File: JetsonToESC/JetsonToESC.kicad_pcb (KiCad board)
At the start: 2 copper layers, 32 x 47.5 mm, 8 parts, among them J1 Conn_01x12, J2 Conn_01x03, U1 ESP32-C3_SUPERMINI_TH, U2 DS18B20

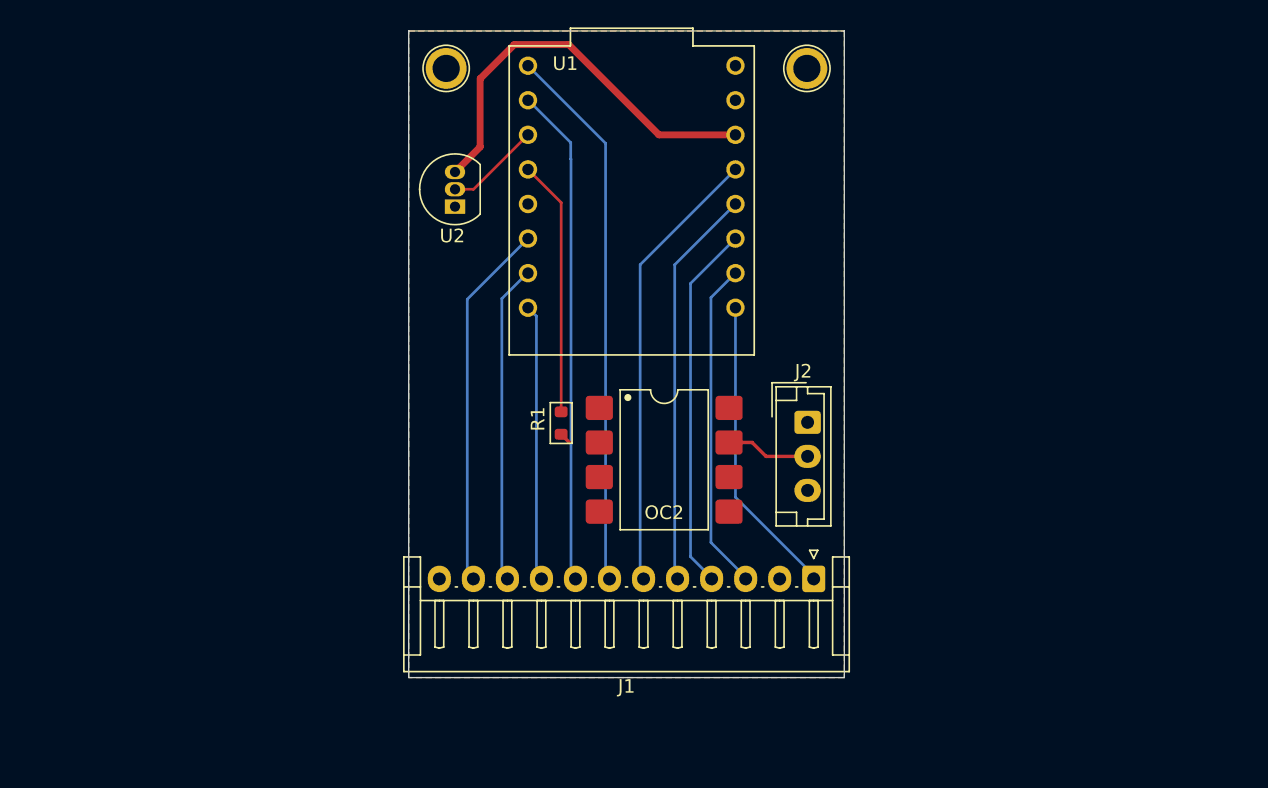
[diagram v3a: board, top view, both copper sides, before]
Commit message: Design almost finished, added hierarchical sheets
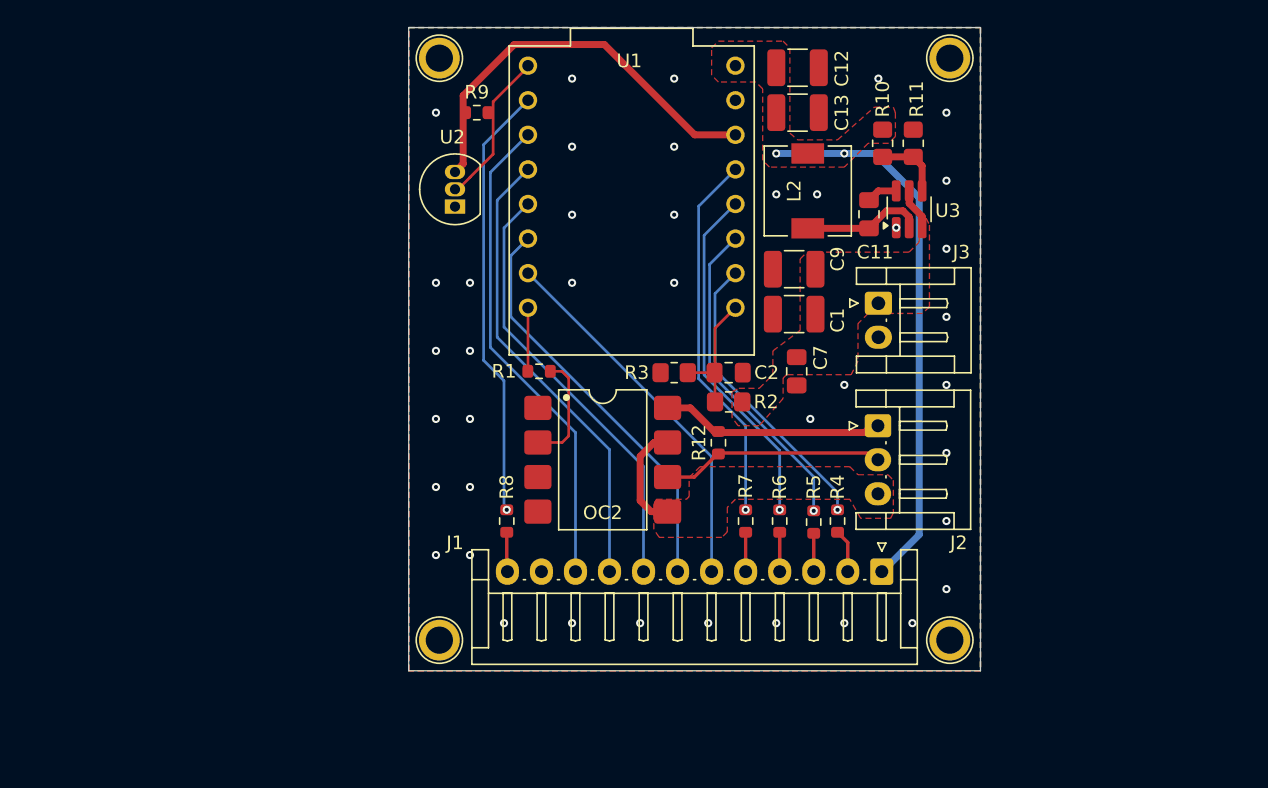
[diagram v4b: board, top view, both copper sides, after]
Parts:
- added C1: 4.7uF, Capacitor_SMD:C_1210_3225Metric_Pad1.33x2.70mm_HandSolder, F.Cu at (166.3, 99.8)
- added C11: 100nF, Capacitor_SMD:C_0805_2012Metric_Pad1.18x1.45mm_HandSolder, F.Cu at (171.8, 92.5)
- added C12: 22uF, Capacitor_SMD:C_1210_3225Metric_Pad1.33x2.70mm_HandSolder, F.Cu at (166.6, 81.7)
- added C13: 22uF, Capacitor_SMD:C_1210_3225Metric_Pad1.33x2.70mm_HandSolder, F.Cu at (166.6, 85.0)
- added C2: 100nF, Capacitor_SMD:C_0805_2012Metric_Pad1.18x1.45mm_HandSolder, F.Cu at (161.5, 104.1)
- added C7: 100nF, Capacitor_SMD:C_0805_2012Metric_Pad1.18x1.45mm_HandSolder, F.Cu at (166.5, 104.0)
- added C9: 4.7uF, Capacitor_SMD:C_1210_3225Metric_Pad1.33x2.70mm_HandSolder, F.Cu at (166.3, 96.5)
- added H3: MountingHole, TestPoint:TestPoint_Plated_Hole_D2.0mm, F.Cu at (140.2, 123.8)
- added H4: MountingHole, TestPoint:TestPoint_Plated_Hole_D2.0mm, F.Cu at (177.8, 123.8)
- added J3: Conn_01x02, Connector_JST:JST_EH_S2B-EH_1x02_P2.50mm_Horizontal, F.Cu at (172.5, 99.0)
- added L2: 6.8uH, Inductor_SMD:L_6.3x6.3_H3, F.Cu at (167.3, 90.8)
- added R10: 100k, Resistor_SMD:R_0805_2012Metric_Pad1.20x1.40mm_HandSolder, F.Cu at (172.8, 87.2)
- added R11: 13.7k, Resistor_SMD:R_0805_2012Metric_Pad1.20x1.40mm_HandSolder, F.Cu at (175.1, 87.2)
- added R12: 4K7, Resistor_SMD:R_0603_1608Metric, F.Cu at (160.8, 109.2)
- added R2: 47K, Resistor_SMD:R_0805_2012Metric_Pad1.20x1.40mm_HandSolder, F.Cu at (161.5, 106.2)
- added R3: 5.1K, Resistor_SMD:R_0805_2012Metric_Pad1.20x1.40mm_HandSolder, F.Cu at (157.5, 104.1)
- added R4: 4K7, Resistor_SMD:R_0603_1608Metric, F.Cu at (169.5, 115.0)
- added R5: 4K7, Resistor_SMD:R_0603_1608Metric, F.Cu at (167.8, 115.1)
- added R6: 4K7, Resistor_SMD:R_0603_1608Metric, F.Cu at (165.2, 115.0)
- added R7: 4K7, Resistor_SMD:R_0603_1608Metric, F.Cu at (162.8, 115.0)
- added R8: 4K7, Resistor_SMD:R_0603_1608Metric, F.Cu at (145.2, 115.0)
- added R9: 4K7, Resistor_SMD:R_0603_1608Metric, F.Cu at (143.0, 85.0)
- added U3: LMR51420XDDCR, Package_TO_SOT_SMD:SOT-23-6_Handsoldering, F.Cu at (174.8, 92.1)
- J2: footprint Connector_JST:JST_EH_B3B-EH-A_1x03_P2.50mm_Vertical -> Connector_JST:JST_EH_S3B-EH_1x03_P2.50mm_Horizontal
- R1: value R -> 220; footprint PCM_Resistor_SMD_AKL:R_0603_1608Metric -> Resistor_SMD:R_0603_1608Metric
- moved H2 10.5 mm to (177.8, 81.0)
- moved J2 5.17 mm to (172.5, 108.0)
- moved J1 5.03 mm to (172.8, 118.7)
- moved OC2 4.51 mm to (152.2, 110.5)
- moved R1 4.13 mm to (147.6, 104.0), turned to 0 degrees
- moved H1 0.90 mm to (140.2, 81.0)
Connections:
- J1 pad 1: LED_TEMP -> 5V
- J1 pad 10: LED_BATT_MED -> BUTTON_STOP
- J1 pad 11: LED_BATT_LOW -> GND
- J1 pad 12: 5V -> LED_TEMP
- J1 pad 2: GND -> LED_BATT_LOW
- J1 pad 3: BUTTON_STOP -> LED_BATT_MED
- J1 pad 4: BUTTON_25% -> LED_BATT_HI
- J1 pad 5: BUTTON_50% -> LED_OVERCURRENT
- J1 pad 6: BUTTON_75% -> BUTTON_100%
- J1 pad 7: BUTTON_100% -> BUTTON_75%
- J1 pad 8: LED_OVERCURRENT -> BUTTON_50%
- J1 pad 9: LED_BATT_HI -> BUTTON_25%
- J2 pad 1: VCC -> VBEC
- J2 pad 3: GND -> GNDB
- OC2 pad 5: GND -> GNDB
- OC2 pad 6: unconnected-(OC2-Pad6) -> ESC_PWM
- OC2 pad 7: ESC_PWM -> GNDB
- OC2 pad 8: VCC -> VBEC
- U1 pad 0: LED_TEMP -> BATT_LEVEL_SENSE
- U1 pad 1: BUTTON_STOP -> Net-(U1-GPIO1)
- U1 pad 10: LED_BATT_LOW -> BUTTON_75%
- U1 pad 2: BUTTON_25% -> Net-(U1-GPIO2)
- U1 pad 20: LED_BATT_MED -> BUTTON_100%
- U1 pad 21: LED_BATT_HI -> PWM
- U1 pad 3: BUTTON_50% -> Net-(U1-GPIO3)
- U1 pad 4: BUTTON_75% -> Net-(U1-GPIO4)
- U1 pad 5: BUTTON_100% -> TEMP_SENSE
- U1 pad 5V: VCC -> 5V
- U1 pad 6: LED_OVERCURRENT -> Net-(U1-GPIO6)
- U1 pad 7: TEMP_SENSE -> BUTTON_STOP
- U1 pad 8: PWM -> BUTTON_25%
- U1 pad 9: unconnected-(U1-GPIO9-Pad9) -> BUTTON_50%
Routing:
- net 5V: track 0.00 -> 40.5 mm, vias 0 -> 2
- net LED_OVERCURRENT: track 36.2 -> 2.89 mm
- net Net-(U1-GPIO6): track 0.00 -> 32.2 mm, vias 0 -> 1
- net Net-(U1-GPIO4): track 0.00 -> 27.6 mm, vias 0 -> 1
- net Net-(U1-GPIO3): track 0.00 -> 25.7 mm, vias 0 -> 1
- net Net-(U1-GPIO2): track 0.00 -> 24.0 mm, vias 0 -> 1
- net LED_BATT_LOW: track 26.6 -> 3.20 mm
- net Net-(U1-GPIO1): track 0.00 -> 21.9 mm, vias 0 -> 1
- net LED_BATT_MED: track 23.0 -> 2.87 mm
- net LED_TEMP: track 22.0 -> 2.91 mm
- net LED_BATT_HI: track 19.9 -> 2.89 mm
- net VBEC: track 0.00 -> 16.4 mm
- net PWM: track 18.8 -> 4.67 mm
- net BUTTON_STOP: track 24.0 -> 36.8 mm
- net BUTTON_100%: track 39.8 -> 28.6 mm
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- added copper zone on F.Cu, net 5V
- added copper zone on F.Cu, net GNDB
- added copper zone on F.Cu, net VBAT
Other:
- board size 32 x 47.5 mm -> 42 x 47.2 mm

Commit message: Start On this Branch
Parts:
- added C3: 100nF, Capacitor_SMD:C_0805_2012Metric_Pad1.18x1.45mm_HandSolder, F.Cu at (117.6, 88.9)
- added R13: 4K7, Resistor_SMD:R_0603_1608Metric, F.Cu at (120.4, 89.3)
- added U4: MCP23018x-x-SS, Package_SO:SSOP-24_5.3x8.2mm_P0.65mm, F.Cu at (194.7, 126.5)
- added U5: ACS759xCB-100B-PFF, Sensor_Current:Allegro_CB_PFF, F.Cu at (141.3, 103.5)

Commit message: Work on current sense and io expansion branch
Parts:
- C11, C2, C7: footprint Capacitor_SMD:C_0805_2012Metric_Pad1.18x1.45mm_HandSolder -> Capacitor_SMD:C_0603_1608Metric
- R2, R3: footprint Resistor_SMD:R_0805_2012Metric_Pad1.20x1.40mm_HandSolder -> Resistor_SMD:R_0603_1608Metric
- moved U4 46.6 mm to (149.6, 114.8), turned to -90 degrees
- moved H3 28.0 mm to (112.5, 127.5)
- moved H1 27.8 mm to (112.5, 82.5)
- moved OC2 10.1 mm to (162.2, 111.8)
- moved R12 8.84 mm to (169.5, 110.5)
- moved R3 5.51 mm to (163.0, 104.5), turned to 90 degrees
- moved R2 5.40 mm to (166.8, 105.2)
- moved R6 4.86 mm to (162.5, 119.0)
- moved R7 4.85 mm to (160.0, 119.0)
- moved R5 4.80 mm to (165.0, 119.0)
- moved J1 4.68 mm to (170.0, 122.5)
- moved R4 4.47 mm to (167.5, 119.0)
- moved H4 3.76 mm to (177.5, 127.5)
- moved U2 3.05 mm to (138.6, 93.2)
- moved U5 3.05 mm to (138.5, 104.8)
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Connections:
- R4 pad 1: LED_BATT_LOW -> LED_OVERCURRENT
- R4 pad 2: Net-(U1-GPIO1) -> Net-(U4-GPB3)
- R5 pad 1: LED_BATT_MED -> LED_OVERCURRENT
- R5 pad 2: Net-(U1-GPIO2) -> Net-(U4-GPB4)
- R6 pad 2: Net-(U1-GPIO3) -> Net-(U4-GPB5)
- R7 pad 1: LED_OVERCURRENT -> LED_BATT_MED
- R7 pad 2: Net-(U1-GPIO4) -> Net-(U4-GPB6)
- R8 pad 1: LED_TEMP -> LED_BATT_LOW
- R8 pad 2: Net-(U1-GPIO6) -> Net-(U4-GPB7)
- U1 pad 1: Net-(U1-GPIO1) -> unconnected-(U1-GPIO1-Pad1)
- U1 pad 10: BUTTON_75% -> unconnected-(U1-GPIO10-Pad10)
- U1 pad 2: Net-(U1-GPIO2) -> unconnected-(U1-GPIO2-Pad2)
- U1 pad 20: BUTTON_100% -> unconnected-(U1-GPIO20-Pad20)
- U1 pad 3: Net-(U1-GPIO3) -> unconnected-(U1-GPIO3-Pad3)
- U1 pad 4: Net-(U1-GPIO4) -> unconnected-(U1-GPIO4-Pad4)
- U1 pad 6: Net-(U1-GPIO6) -> unconnected-(U1-GPIO6-Pad6)
- U1 pad 7: BUTTON_STOP -> unconnected-(U1-GPIO7-Pad7)
- U1 pad 8: BUTTON_25% -> I2C_SDA
- U1 pad 9: BUTTON_50% -> I2C_SCL
- U4 pad 5: LED_OVERCURRENT -> Net-(U4-GPB3)
- U4 pad 6: LED_OVERCURRENT -> Net-(U4-GPB4)
- U4 pad 7: LED_BATT_HI -> Net-(U4-GPB5)
- U4 pad 8: LED_BATT_MED -> Net-(U4-GPB6)
- U4 pad 9: LED_BATT_LOW -> Net-(U4-GPB7)
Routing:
- net BUTTON_STOP: track 36.8 -> 0.00 mm
- net BUTTON_25%: track 34.4 -> 0.00 mm
- net BUTTON_50%: track 33.0 -> 0.00 mm
- net Net-(U1-GPIO6): track 32.2 -> 0.00 mm, vias 1 -> 0
- net BUTTON_75%: track 30.3 -> 0.00 mm
- net BUTTON_100%: track 28.6 -> 0.00 mm
- net Net-(U1-GPIO4): track 27.6 -> 0.00 mm, vias 1 -> 0
- net Net-(U1-GPIO3): track 25.7 -> 0.00 mm, vias 1 -> 0
- net Net-(U1-GPIO2): track 24.0 -> 0.00 mm, vias 1 -> 0
- net Net-(U1-GPIO1): track 21.9 -> 0.00 mm, vias 1 -> 0
- net VBEC: track 16.4 -> 0.00 mm
- net ESC_PWM: track 16.4 -> 0.00 mm
- net Net-(OC2-Pad2): track 8.27 -> 0.00 mm
- net GNDB: track 8.25 -> 0.00 mm
- net 5V: track 40.5 -> 45.6 mm
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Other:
- board size 42 x 47.2 mm -> 70 x 50 mm

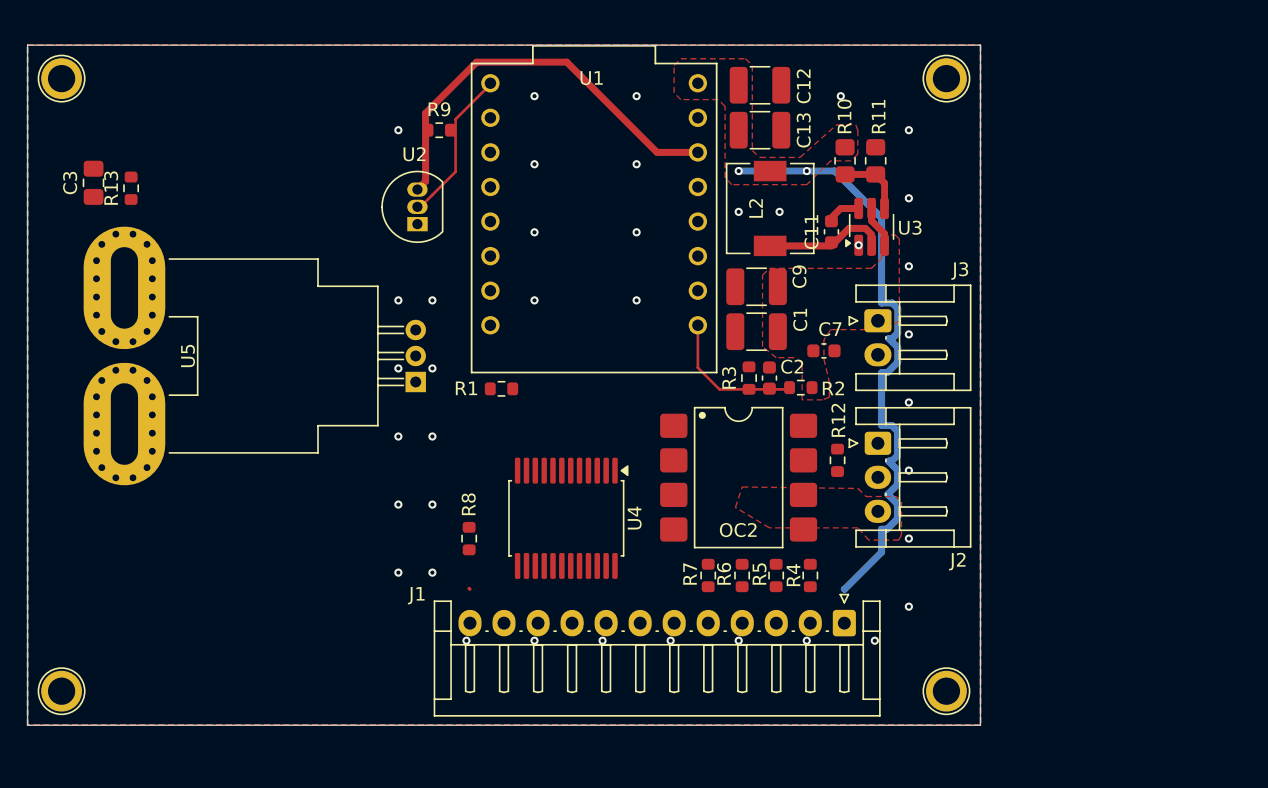
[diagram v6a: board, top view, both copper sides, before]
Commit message: Updated routing for IO Expander and Hall Sensor
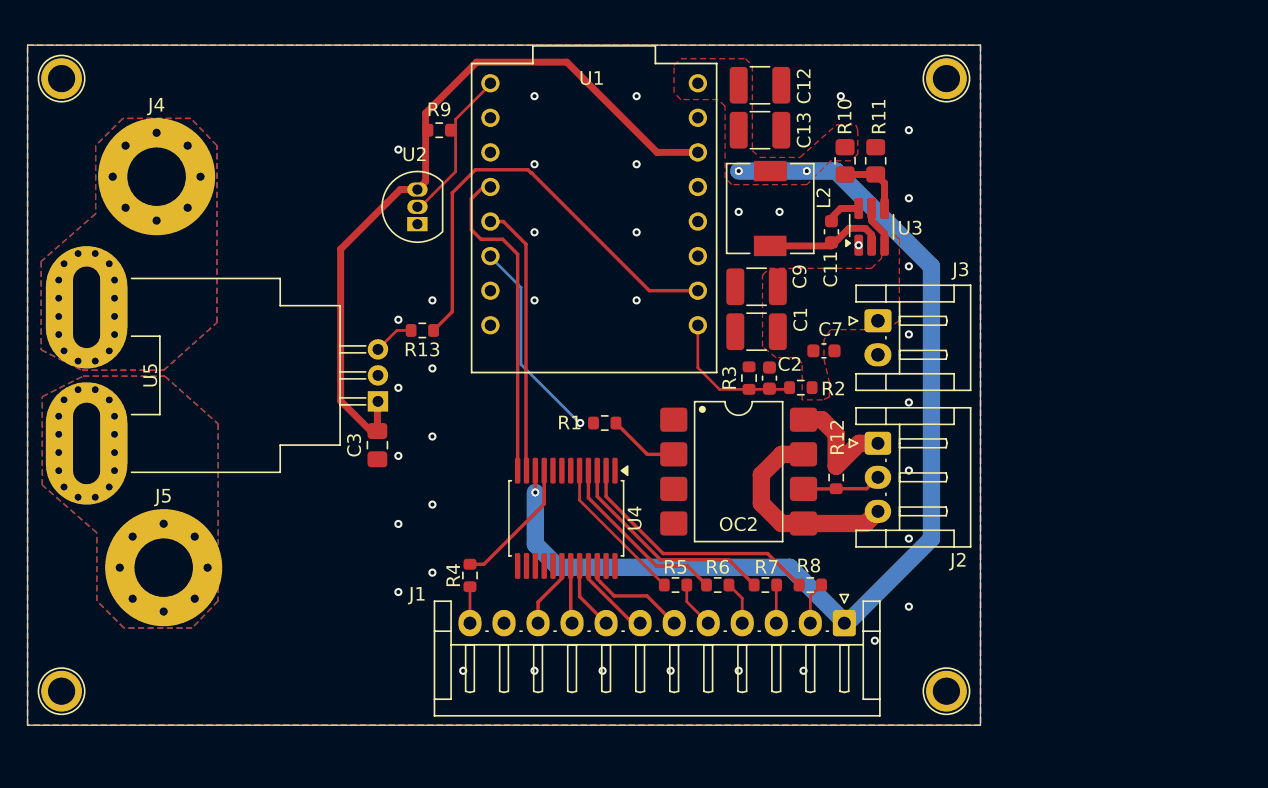
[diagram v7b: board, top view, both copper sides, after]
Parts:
- added J4: Screw_Terminal_01x01, MountingHole:MountingHole_4.3mm_M4_Pad_Via, F.Cu at (119.5, 89.7)
- added J5: Screw_Terminal_01x01, MountingHole:MountingHole_4.3mm_M4_Pad_Via, F.Cu at (120.0, 118.4)
- moved C3 28.4 mm to (135.7, 109.4)
- moved R8 25.3 mm to (167.5, 119.7), turned to 180 degrees
- moved R4 25.0 mm to (142.5, 119.0)
- moved R13 23.8 mm to (139.0, 101.0), turned to 180 degrees
- moved R1 7.99 mm to (152.4, 107.8)
- moved R5 7.42 mm to (157.6, 119.7), turned to 180 degrees
- moved R7 4.26 mm to (164.2, 119.7), turned to 180 degrees
- moved U5 3.12 mm to (135.7, 106.2)
- moved R6 1.92 mm to (160.7, 119.7), turned to 180 degrees
- moved R12 1.26 mm to (169.4, 111.8)
- moved OC2 0.44 mm to (162.2, 111.4)
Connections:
- R4 pad 1: LED_OVERCURRENT -> LED_TEMP
- R4 pad 2: Net-(U4-GPB3) -> Net-(U4-GPB7)
- R5 pad 2: Net-(U4-GPB4) -> Net-(U4-GPB3)
- R6 pad 2: Net-(U4-GPB5) -> Net-(U4-GPB2)
- R7 pad 2: Net-(U4-GPB6) -> Net-(U4-GPB1)
- R8 pad 2: Net-(U4-GPB7) -> Net-(U4-GPB0)
- U1 pad 1: unconnected-(U1-GPIO1-Pad1) -> CURRENT_SENSE
- U1 pad 10: unconnected-(U1-GPIO10-Pad10) -> PWM
- U1 pad 20: unconnected-(U1-GPIO20-Pad20) -> UART_TX
- U1 pad 21: PWM -> UART_RX
- U4 pad 2: unconnected-(U4-GPB0-Pad2) -> Net-(U4-GPB0)
- U4 pad 3: unconnected-(U4-GPB1-Pad3) -> Net-(U4-GPB1)
- U4 pad 4: unconnected-(U4-GPB2-Pad4) -> Net-(U4-GPB2)
- U4 pad 6: Net-(U4-GPB4) -> unconnected-(U4-GPB4-Pad6)
- U4 pad 7: Net-(U4-GPB5) -> unconnected-(U4-GPB5-Pad7)
- U4 pad 8: Net-(U4-GPB6) -> unconnected-(U4-GPB6-Pad8)
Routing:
- net CURRENT_SENSE: track 0.00 -> 33.1 mm
- net 5V: track 45.6 -> 76.6 mm, vias 2 -> 3
- net 3V3: track 30.2 -> 55.2 mm
- net I2C_SDA: track 0.00 -> 24.1 mm
- net I2C_SCL: track 0.00 -> 20.0 mm
- net Net-(U4-GPB0): track 0.00 -> 18.8 mm
- net Net-(U4-GPB1): track 0.00 -> 16.1 mm
- net GNDB: track 0.00 -> 15.4 mm
- net PWM: track 0.01 -> 15.3 mm, vias 0 -> 1
- net Net-(U4-GPB2): track 0.00 -> 13.3 mm
- net Net-(U4-GPB3): track 0.00 -> 11.0 mm
- net Net-(U4-GPB7): track 0.00 -> 9.73 mm
- net VBEC: track 0.00 -> 8.97 mm
- net BUTTON_100%: track 0.00 -> 7.95 mm
- net BUTTON_75%: track 0.00 -> 6.10 mm
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- added copper zone on B.Cu, net VBAT_IN
- added copper zone on F.Cu, net VBAT_IN
- added copper zone on B.Cu, net VBAT_OUT
- added copper zone on F.Cu, net VBAT_OUT
- removed copper zone on F.Cu, net GNDB
